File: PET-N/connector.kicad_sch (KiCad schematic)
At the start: 25 parts, among them J1 Extended_PET_keyboard_connect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, SW3 NC ($10), SW320 S LOCK, SW67 NC ($0A)

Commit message: working on new layout
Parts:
- added D1: 1N4448, Diode_SMD:D_SOD-323_HandSoldering, symbol PCM_Diode_AKL:1N4448
- added JP5: SolderJumper_2_Bridged, Jumper:SolderJumper-2_P1.3mm_Open_RoundedPad1.0x1.5mm, symbol Jumper:SolderJumper_2_Open
- added R3: 10k, Resistor_SMD:R_0603_1608Metric, symbol Device:R
- added U9: 74HCT00, Package_SO:SOIC-14_3.9x8.7mm_P1.27mm, symbol 74xx:74HCT00
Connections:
- net VCC: now also R3.2
- net cR1: now also D1.2 (A), JP5.1 (A), U9.1, U9.2
- new net: JP5.2 (B), R3.1, U9.12, U9.13
- new net: U9.10, U9.3, U9.5
- new net /RESLED: U9.8
- new net /RESOUT: D1.1 (K), U9.4, U9.9
- new net /RESSCAN: U9.6
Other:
- note added: "Experimental /RES circuit: /RESOUT from kbd controller triggers host reset only; host reset resets kbd/led ctrl as well"

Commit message: layout work
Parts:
- added unit 4 of U9
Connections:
- net at JP5.2 (B), R3.1: now also U9.12, U9.13; no longer U9.12, U9.13

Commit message: add orientation marker for backlight LEDs and move to 3.1B
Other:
- note added: "CBM-KEYB-PETN-3.1B-20260405"
- note removed: "CBM-KEYB-PETN-3.1A-20260130"
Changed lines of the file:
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@@
 		)
 	)
-	(text "CBM-KEYB-PETN-3.1A-20260130"
+	(text "CBM-KEYB-PETN-3.1B-20260405"
 		(exclude_from_sim no)
 		(at 230.505 173.99 0)

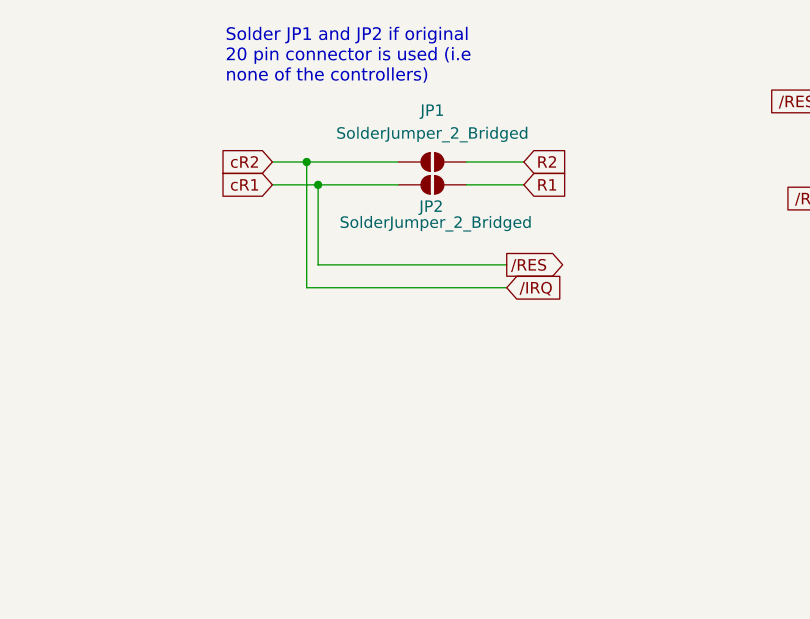
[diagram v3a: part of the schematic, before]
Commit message: add irq/nmi out
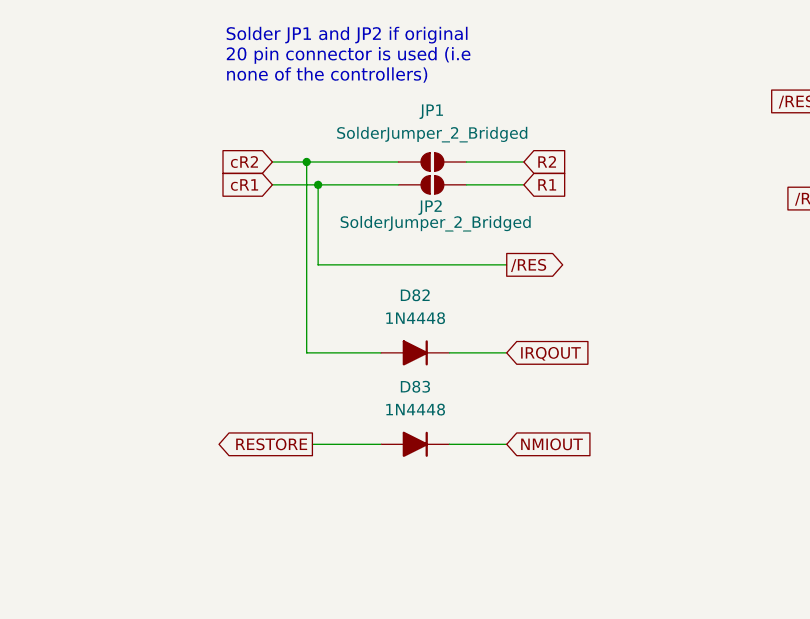
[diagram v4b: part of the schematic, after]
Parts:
- added D82, D83: 1N4448, Diode_SMD:D_SOD-323_HandSoldering, symbol PCM_Diode_AKL:1N4448
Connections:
- net RESTORE: now also D83.2 (A)
- net cR2: now also D82.2 (A)
- new net IRQOUT: D82.1 (K)
- new net NMIOUT: D83.1 (K)
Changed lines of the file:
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@@
+	(wire
+		(pts
+			(xy 154.94 149.86) (xy 161.29 149.86)
+		)
+		(stroke
+			(width 0)
+			(type default)
+		)
+	)
 	(wire
 		(pts
@@
 	(wire
 		(pts
+			(xy 139.065 139.7) (xy 147.32 139.7)
+		)
+		(stroke
+			(width 0)
+			(type default)
+		)
+	)
+	(wire
+		(pts
 			(xy 47.625 74.549) (xy 48.895 74.549)
 		)
@@
 	(wire
 		(pts
-			(xy 161.29 132.461) (xy 139.065 132.461)
+			(xy 139.7 149.86) (xy 147.32 149.86)
 		)
 		(stroke
@@
 	(wire
 		(pts
-			(xy 139.065 132.461) (xy 139.065 118.491)
+			(xy 139.065 139.7) (xy 139.065 118.491)
 		)
 		(stroke
@@
 		(pts
 			(xy 55.245 116.84) (xy 57.785 116.84)
+		)
+		(stroke
+			(width 0)
+			(type default)
+		)
+	)
+	(wire
+		(pts
+			(xy 154.94 139.7) (xy 161.29 139.7)
 		)
 		(stroke
@@
 		)
 	)
-	(global_label "{slash}IRQ"
-		(shape input)
-		(at 161.29 132.461 0)
-		(fields_autoplaced yes)
-		(effects
-			(font
-				(size 1.27 1.27)
-			)
-			(justify left)
-		)
-		(property "Intersheetrefs" "${INTERSHEET_REFS}"
-			(at 168.1568 132.461 0)
+	(global_label "IRQOUT"
+		(shape input)
+		(at 161.29 139.7 0)
+		(fields_autoplaced yes)
+		(effects
+			(font
+				(size 1.27 1.27)
+			)
+			(justify left)
+		)
+		(property "Intersheetrefs" "${INTERSHEET_REFS}"
+			(at 170.4549 139.7 0)
 			(effects
 				(font
@@
 					(size 1.27 1.27)
 				)
+				(hide yes)
+			)
+		)
+	)
+	(global_label "NMIOUT"
+		(shape input)
+		(at 161.29 149.86 0)
+		(fields_autoplaced yes)
+		(effects
+			(font
+				(size 1.27 1.27)
+			)
+			(justify left)
+		)
+		(property "Intersheetrefs" "${INTERSHEET_REFS}"
+			(at 170.6363 149.86 0)
+			(effects
+				(font
+					(size 1.27 1.27)
+				)
+				(justify left)
 				(hide yes)
 			)
@@
 				)
 				(justify left)
+				(hide yes)
+			)
+		)
+	)
+	(global_label "RESTORE"
+		(shape output)
+		(at 139.7 149.86 180)
+		(fields_autoplaced yes)
+		(effects
+			(font
+				(size 1.27 1.27)
+			)
+			(justify right)
+		)
+		(property "Intersheetrefs" "${INTERSHEET_REFS}"
+			(at 129.0234 149.86 0)
+			(effects
+				(font
+					(size 1.27 1.27)
+				)
+				(justify right)
 				(hide yes)
 			)
@@
 	)
 	(symbol
+		(lib_id "PCM_Diode_AKL:1N4448")
+		(at 151.13 139.7 0)
+		(unit 1)
+		(exclude_from_sim no)
+		(in_bom yes)
+		(on_board yes)
+		(dnp no)
+		(fields_autoplaced yes)
+		(property "Reference" "D82"
+			(at 151.13 133.35 0)
+			(effects
+				(font
+					(size 1.27 1.27)
+				)
+			)
+		)
+		(property "Value" "1N4448"
+			(at 151.13 135.89 0)
+			(effects
+				(font
+					(size 1.27 1.27)
+				)
+			)
+		)
+		(property "Footprint" "Diode_SMD:D_SOD-323_HandSoldering"
+			(at 151.13 139.7 0)
+			(effects
+				(font
+					(size 1.27 1.27)
+				)
+				(hide yes)
+			)
+		)
+		(property "Datasheet" "https://datasheet.octopart.com/1N4448TR-ON-Semiconductor-datasheet-42765246.pdf"
+			(at 151.13 139.7 0)
+			(effects
+				(font
+					(size 1.27 1.27)
+				)
+				(hide yes)
+			)
+		)
+		(property "Description" "DO-35 Diode, Small Signal, Fast Switching, 75V, 150mA, 4ns, Alternate KiCad Library"
+			(at 151.13 139.7 0)
+			(effects
+				(font
+					(size 1.27 1.27)
+				)
+				(hide yes)
+			)
+		)
+		(pin "1"
+		)
+		(pin "2"
+		)
+		(instances
+			(project "petkn"
+				(path "/a0727808-af70-4056-b2ee-ab828c2acfbd/ec43c8d3-5460-4a1b-a32f-0e2b09b685ff"
+					(reference "D82")
+					(unit 1)
+				)
+			)
+		)
+	)
+	(symbol
 		(lib_id "Jumper:SolderJumper_2_Open")
 		(at 43.815 65.659 0)
@@
 					(unit 1)
 				)
+			)
+		)
+	)
+	(symbol
+		(lib_id "PCM_Diode_AKL:1N4448")
+		(at 151.13 149.86 0)
+		(unit 1)
+		(exclude_from_sim no)
+		(in_bom yes)
+		(on_board yes)
+		(dnp no)
+		(fields_autoplaced yes)
+		(property "Reference" "D83"
+			(at 151.13 143.51 0)
+			(effects
+				(font
+					(size 1.27 1.27)
+				)
+			)
+		)
+		(property "Value" "1N4448"
+			(at 151.13 146.05 0)
+			(effects
+				(font
+					(size 1.27 1.27)
+				)
+			)
+		)
+		(property "Footprint" "Diode_SMD:D_SOD-323_HandSoldering"
+			(at 151.13 149.86 0)
+			(effects
+				(font
+					(size 1.27 1.27)
+				)
+				(hide yes)
+			)
+		)
+		(property "Datasheet" "https://datasheet.octopart.com/1N4448TR-ON-Semiconductor-datasheet-42765246.pdf"
+			(at 151.13 149.86 0)
+			(effects
+				(font
+					(size 1.27 1.27)
+				)
+				(hide yes)
+			)
+		)
+		(property "Description" "DO-35 Diode, Small Signal, Fast Switching, 75V, 150mA, 4ns, Alternate KiCad Library"
+			(at 151.13 149.86 0)
+			(effects
+				(font
+					(size 1.27 1.27)
+				)
+				(hide yes)
+			)
+		)
+		(pin "1"
+		)
+		(pin "2"
+		)
+		(instances
+			(project "petkn"
+				(path "/a0727808-af70-4056-b2ee-ab828c2acfbd/ec43c8d3-5460-4a1b-a32f-0e2b09b685ff"
+					(reference "D83")
+					(unit 1)
+				)
